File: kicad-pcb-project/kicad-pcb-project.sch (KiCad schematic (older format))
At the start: 157 parts, among them SW1 SW_Push, U1 ATmega32U4-AU, Y1 16MHz

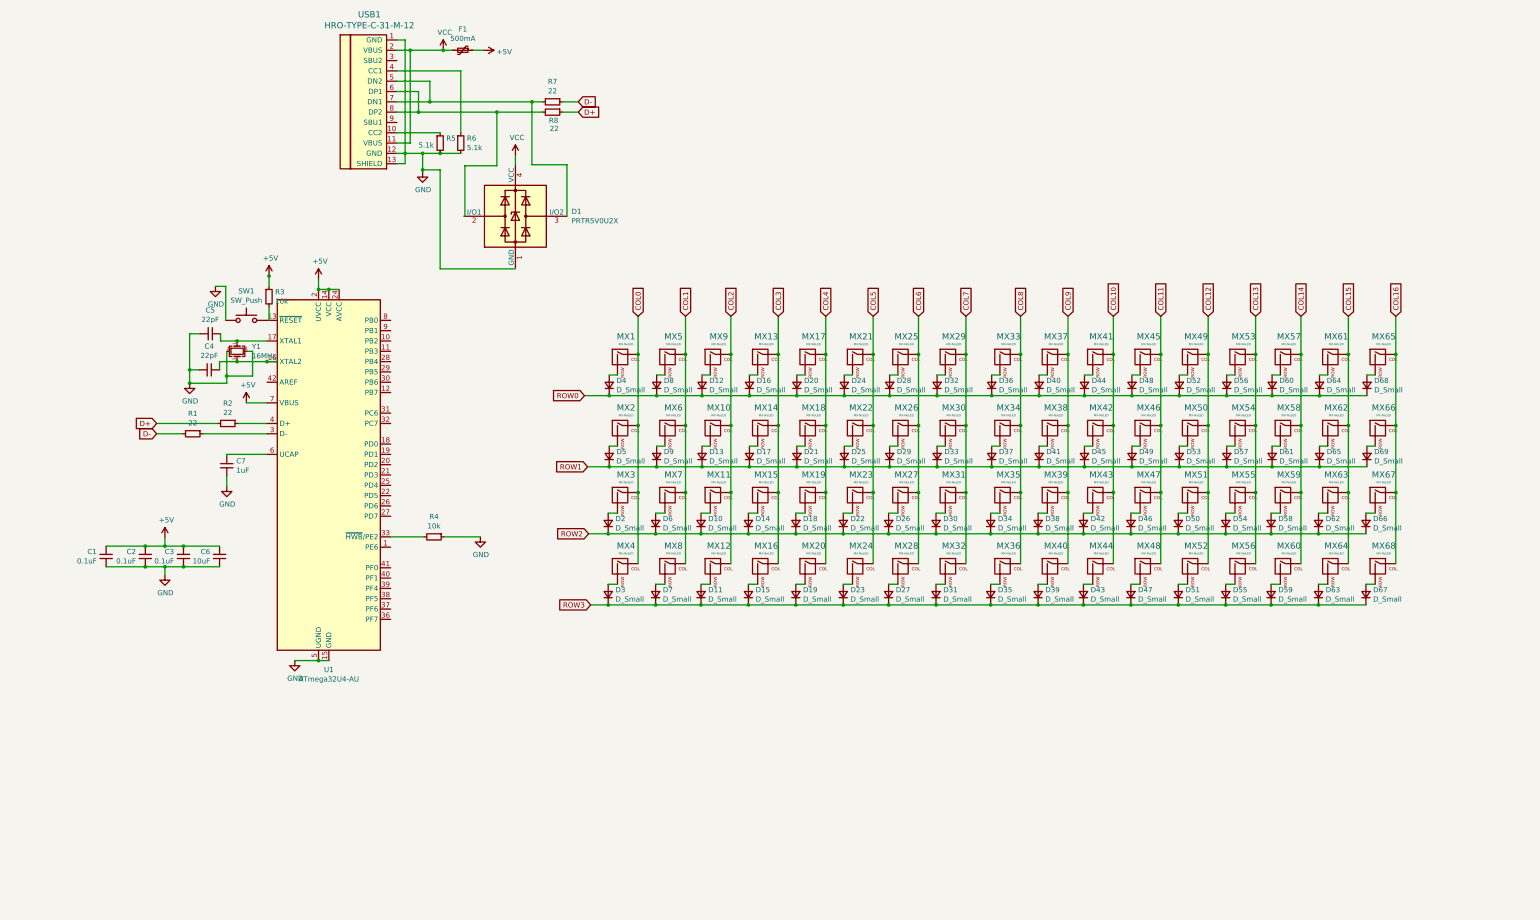
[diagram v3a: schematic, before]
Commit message: adding additional layouts to switch matrix
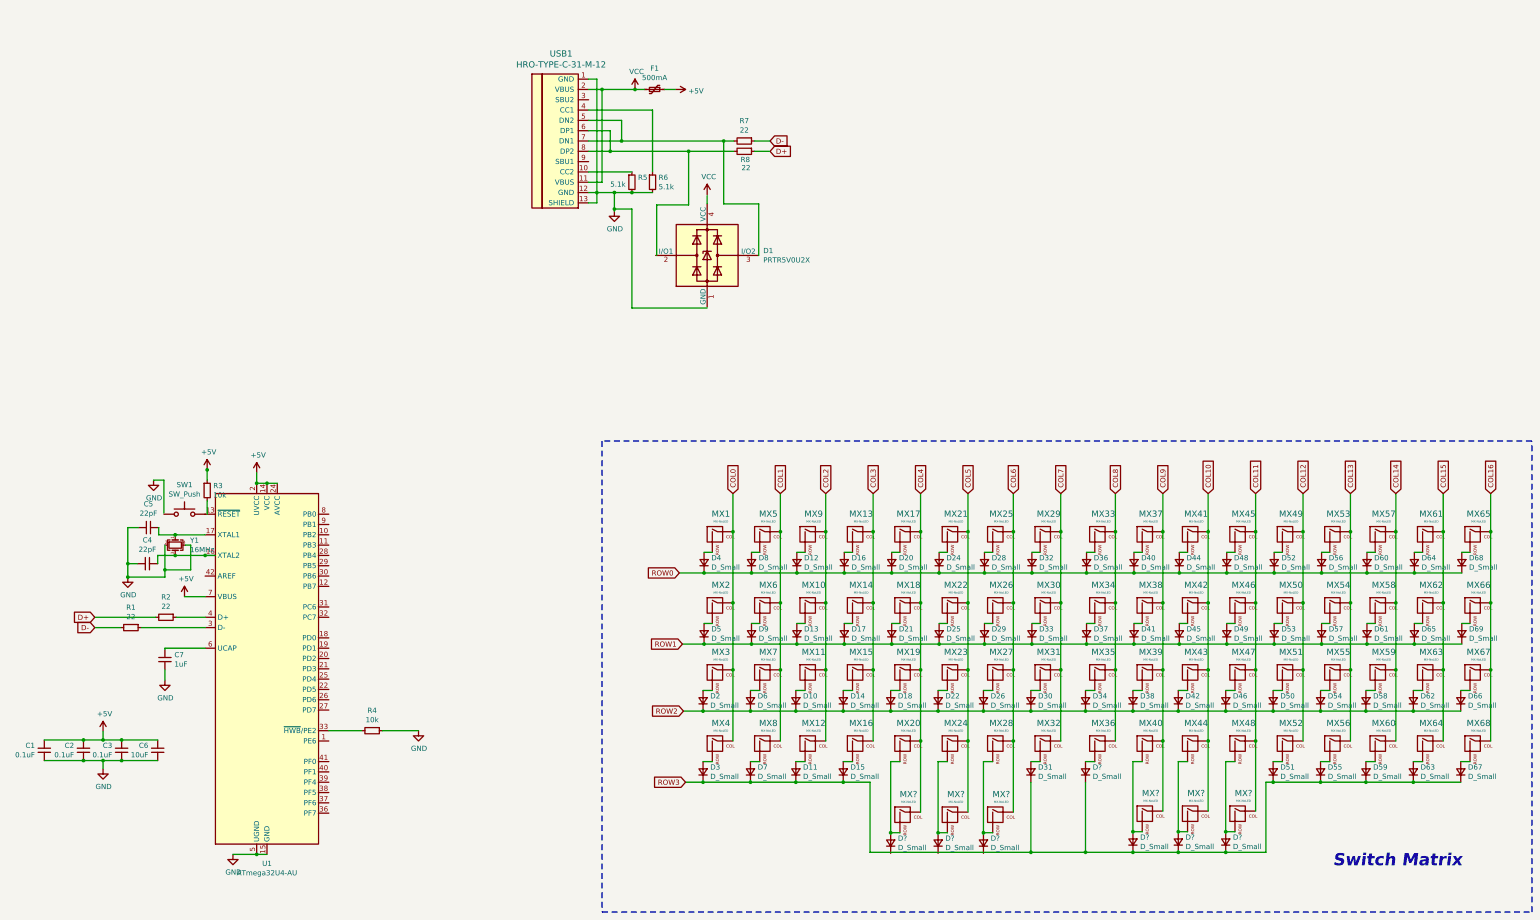
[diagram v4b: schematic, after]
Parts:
- removed D19, D23, D27, D35, D39, D43, D47: D_Small, Diode_SMD:D_SOD-123, symbol Device:D_Small
- added D? (x7): D_Small, Diode_SMD:D_SOD-123, symbol Device:D_Small
- added MX? (x6): MX-NoLED, keyswitches:Kailh_socket_MX, symbol MX_Alps_Hybrid:MX-NoLED
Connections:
- net COL10: now also MX?.1 (COL)
- net COL11: now also MX?.1 (COL)
- net COL4: now also MX?.1 (COL)
- net COL5: now also MX?.1 (COL)
- net COL6: now also MX?.1 (COL)
- net COL9: now also MX?.1 (COL)
- net ROW3: now also D?.1 (K), D?.1 (K), D?.1 (K), D?.1 (K)
- net at MX20.2 (ROW): now also D?.2 (A), MX?.2 (ROW)
- net at MX24.2 (ROW): now also D?.2 (A), MX?.2 (ROW)
- net at MX28.2 (ROW): now also D?.2 (A), MX?.2 (ROW)
- net at MX36.2 (ROW): now also D?.2 (A)
- net at MX40.2 (ROW): now also D?.2 (A), MX?.2 (ROW)
- net at MX44.2 (ROW): now also D?.2 (A), MX?.2 (ROW)
- net at MX48.2 (ROW): now also D?.2 (A), MX?.2 (ROW)
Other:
- note added: "Switch Matrix\n"
- moved on the sheet: C1, C2, C3, C4, C5, C6, C7, D1, D10, D11, D12, D13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

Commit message: adding pdf of schematic and .gitignore file
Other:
- note added: "MCU"
- note added: "USB-C"
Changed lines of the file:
@@
 Text Notes 13920 8870 0    118  Italic 24
 Switch Matrix\n
+Wire Notes Line width 20
+	5570 4610 5570 9440
+Wire Notes Line width 20
+	5570 9440 830  9440
+Wire Notes Line width 20
+	830  9440 830  4610
+Wire Notes Line width 20
+	830  4610 5570 4610
+Text Notes 1970 9100 0    118  Italic 24
+MCU
+Wire Notes Line width 20
+	9070 790  9070 3710
+Wire Notes Line width 20
+	9070 3710 5490 3710
+Wire Notes Line width 20
+	5490 3710 5490 790
+Wire Notes Line width 20
+	5490 790  9070 790
+Text Notes 8180 3490 0    118  Italic 24
+USB-C
 $EndSCHEMATC

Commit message: updating schematic to include the soph68 by nicoles components ex-switch grid
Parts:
- removed C1, C2, C3: 0.1uF, Capacitor_SMD:C_0805_2012Metric, symbol Device:C_Small
- removed C4, C5: 22pF, Capacitor_SMD:C_0805_2012Metric, symbol Device:C_Small
- removed C6: 10uF, Capacitor_SMD:C_0805_2012Metric, symbol Device:C_Small
- removed C7: 1uF, Diode_SMD:D_SOD-123, symbol Device:C_Small
- removed D1: PRTR5V0U2X, Diode_SMD:D_SOD-123, symbol Power_Protection:PRTR5V0U2X
- removed D?: D_Small, Diode_SMD:D_SOD-123, symbol Device:D_Small
- removed MX?: MX-NoLED, keyswitches:Kailh_socket_MX, symbol MX_Alps_Hybrid:MX-NoLED
- removed R1, R2, R7, R8: 22, Resistor_SMD:R_0805_2012Metric, symbol Device:R_Small
- removed R3, R4: 10k, Resistor_SMD:R_0805_2012Metric, symbol Device:R_Small
- removed R5, R6: 5.1k, Resistor_SMD:R_0805_2012Metric, symbol Device:R_Small
- removed SW1: SW_Push, random-keyboard-parts:SKQG-1155865, symbol Switch:SW_Push
- removed U1: ATmega32U4-AU, Package_QFP:TQFP-44_10x10mm_P0.8mm, symbol MCU_Microchip_ATmega:ATmega32U4-AU
- removed USB1: HRO-TYPE-C-31-M-12, Type-C:HRO-TYPE-C-31-M-12-Assembly, symbol Type-C:HRO-TYPE-C-31-M-12
- removed Y1: 16MHz, Crystal:Crystal_SMD_3225-4Pin_3.2x2.5mm, symbol Device:Crystal_GND24_Small
- added CB1, CB2, CB4, CB7, CBT1, CRST1: 100nF, Capacitor_SMD:C_0402_1005Metric, symbol Device:C_Small
- added CB3, CB8: 4.7uF, Capacitor_SMD:C_0402_1005Metric, symbol Device:C_Small
- added CB5: 10n, Capacitor_SMD:C_0402_1005Metric, symbol Device:C_Small
- added CB6: 1uF, Capacitor_SMD:C_0402_1005Metric, symbol Device:C_Small
- added CSH1: 4.7nF, Capacitor_SMD:C_0805_2012Metric, symbol Device:C_Small
- added CSI1, CSO1: 1u, Capacitor_SMD:C_0805_2012Metric, symbol Device:C_Small
- added D?: D_Small, Diode_SMD:D_SOD-123, symbol Device:D_Small
- added DF1: P6SMB6.8CA, Diode_SMD:D_SMB, symbol Device:D_TVS
- added DS1: SM4007, Diode_SMD:D_MELF, symbol Diode:SM4007
- added J1: STLINK_6_Pin, Connectors:2X3_LOCK, symbol soph68-rescue:STLINK_6_Pin-SparkFun-Connectors
- added MX?: MX-NoLED, keyswitches:Kailh_socket_MX, symbol MX_Alps_Hybrid:MX-NoLED
- added QLED1: AO3400A, Package_TO_SOT_SMD:SOT-23, symbol Device:Q_NMOS_GSD
- added RBT1: 10k, Resistor_SMD:R_0805_2012Metric, symbol Device:R_Small
- added RCC1, RCC2: 5.1k, Resistor_SMD:R_0805_2012Metric, symbol Device:R_Small
- added RGND1: R_Small, Resistor_SMD:R_1206_3216Metric, symbol Device:R_Small
- added RLED1: 100R, Resistor_SMD:R_0402_1005Metric, symbol Device:R_Small
- added RSH1: 1M, Resistor_SMD:R_0805_2012Metric, symbol Device:R_Small
- added RSI1: 1M, Capacitor_SMD:C_0805_2012Metric, symbol Device:R_Small
- added SWBT1, SWRST1: SW_Push, Button_Switch_SMD:SW_SPST_SKQG_WithStem, symbol Switch:SW_Push
- added U1: SRV05-4, Package_TO_SOT_SMD:SOT-23-6, symbol Power_Protection:SRV05-4
- added U2: STM32F072CBTx, Package_QFP:LQFP-48_7x7mm_P0.5mm, symbol MCU_ST_STM32F0:STM32F072CBTx
- added U3: AMS1117-5.0, Package_TO_SOT_SMD:SOT-223-3_TabPin2, symbol Regulator_Linear:AMS1117-5.0
- added USB1: USB_C_GCT_USB4085-Type-C, Connector_USB:USB_C_Receptacle_GCT_USB4085, symbol soph68-rescue:USB_C_GCT_USB4085-Type-C-discipline-pcb-rescue
- F1: value 500mA -> 1.5A trip PTC; footprint Fuse:Fuse_1206_3216Metric -> Fuse:Fuse_1812_4532Metric; JLCCode (none) -> C84140
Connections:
- net labels added: +3.3V, BOOT0, GNDD, LED-, LED_PWM, NRST, SWCLK, SWDIO, VBAT, VBUS, VDD, VDDA, VDDIO2, col0, col1, col10, col11, col12, col13, col14, col15, col16, col2, col3, col4, col5, col6, col7, col8, col9, row0, row1, row2, row3, row4
- net labels removed: VCC
- wire segments 313 -> 391
- no-connect marks 0 -> 14
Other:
- note added: "Boot Switch"
- note added: "LED PWM"
- note added: "Power protection"
- note added: "Reset Switch"
- note added: "Serial Programmer"
- note added: "USB Connector"
- note added: "USB ESD"
- note removed: "USB-C"
- moved on the sheet: D11, D2, D22, D26, D28, D29, D3, D30, D31, D32, D33, D36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
